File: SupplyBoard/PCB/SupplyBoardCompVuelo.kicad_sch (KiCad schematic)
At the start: 3 parts, among them J1 Conn_01x02, J2 NebulaConnector, SW1 SW_SPDT

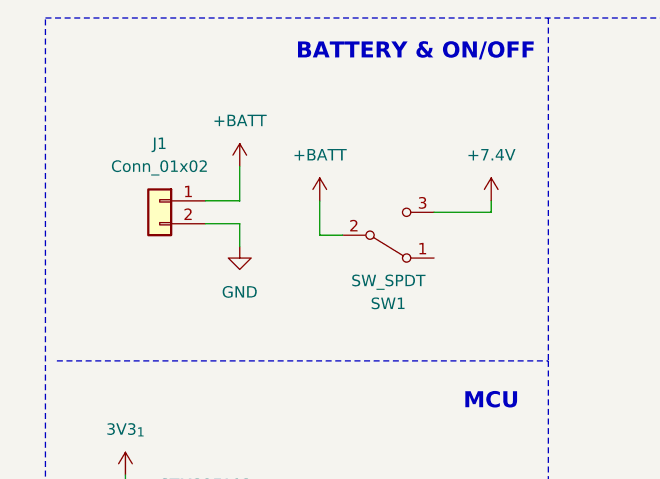
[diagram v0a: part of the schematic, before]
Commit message: Supply & Coms-Sensor Board
la organizacion de los componentes presentes en las placas, se quedaran de esa manera, se espera que en la serigrafia se incluyan los logos de los patrocinadores, ademas se incluyo la carpeta 3D la cual contiene modelos en 3D de las dos placas, con serigrafia y componentes incluidos y ya
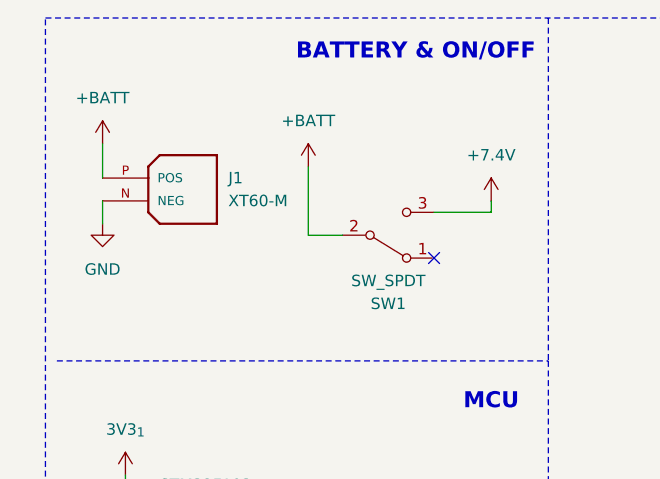
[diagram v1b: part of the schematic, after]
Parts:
- removed J1: Conn_01x02, Connector_AMASS:AMASS_XT30U-F_1x02_P5.0mm_Vertical, symbol Connector_Generic:Conn_01x02
- added J1: XT60-M, CompVuelo:AMASS_XT60-M, symbol CompVuelo:XT60-M
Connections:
- net +BATT: now also J1.P (POS)
- net GND: now also J1.N (NEG)
- no-connect marks 0 -> 1
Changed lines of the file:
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@@
 		)
+	)
+	(no_connect
+		(at 58.42 41.91)
 	)
 	(polyline
@@
 	(wire
 		(pts
-			(xy 36.83 31.75) (xy 36.83 35.56)
+			(xy 21.59 29.21) (xy 21.59 33.02)
 		)
 		(stroke
@@
 		)
 	)
+	(wire
+		(pts
+			(xy 44.45 39.37) (xy 48.26 39.37)
+		)
+		(stroke
+			(width 0)
+			(type default)
+		)
+	)
 	(polyline
 		(pts
@@
 	(wire
 		(pts
-			(xy 36.83 38.1) (xy 33.02 38.1)
-		)
-		(stroke
-			(width 0)
-			(type default)
-		)
-	)
-	(wire
-		(pts
 			(xy 132.08 48.26) (xy 129.54 48.26)
 		)
@@
 	(wire
 		(pts
-			(xy 36.83 35.56) (xy 33.02 35.56)
-		)
-		(stroke
-			(width 0)
-			(type default)
-		)
-	)
-	(wire
-		(pts
 			(xy 58.42 36.83) (xy 64.77 36.83)
 		)
@@
 		(pts
 			(xy 57.15 72.39) (xy 55.88 72.39)
-		)
-		(stroke
-			(width 0)
-			(type default)
-		)
-	)
-	(wire
-		(pts
-			(xy 45.72 39.37) (xy 48.26 39.37)
 		)
 		(stroke
@@
 	(wire
 		(pts
-			(xy 45.72 35.56) (xy 45.72 39.37)
-		)
-		(stroke
-			(width 0)
-			(type default)
-		)
-	)
-	(wire
-		(pts
-			(xy 36.83 38.1) (xy 36.83 40.64)
+			(xy 44.45 31.75) (xy 44.45 39.37)
+		)
+		(stroke
+			(width 0)
+			(type default)
+		)
+	)
+	(wire
+		(pts
+			(xy 21.59 35.56) (xy 21.59 38.1)
 		)
 		(stroke
@@
 	)
 	(symbol
+		(lib_id "CompVuelo:XT60-M")
+		(at 26.67 35.56 0)
+		(unit 1)
+		(exclude_from_sim no)
+		(in_bom yes)
+		(on_board yes)
+		(dnp no)
+		(fields_autoplaced yes)
+		(property "Reference" "J1"
+			(at 35.56 33.0199 0)
+			(effects
+				(font
+					(size 1.27 1.27)
+				)
+				(justify left)
+			)
+		)
+		(property "Value" "XT60-M"
+			(at 35.56 35.5599 0)
+			(effects
+				(font
+					(size 1.27 1.27)
+				)
+				(justify left)
+			)
+		)
+		(property "Footprint" "CompVuelo:AMASS_XT60-M"
+			(at 26.67 35.56 0)
+			(effects
+				(font
+					(size 1.27 1.27)
+				)
+				(justify bottom)
+				(hide yes)
+			)
+		)
+		(property "Datasheet" ""
+			(at 26.67 35.56 0)
+			(effects
+				(font
+					(size 1.27 1.27)
+				)
+				(hide yes)
+			)
+		)
+		(property "Description" ""
+			(at 26.67 35.56 0)
+			(effects
+				(font
+					(size 1.27 1.27)
+				)
+				(hide yes)
+			)
+		)
+		(pin "N"
+		)
+		(pin "P"
+		)
+		(instances
+			(project ""
+				(path "/2119c5ce-afa8-4b00-8fd4-fc653d4beb45"
+					(reference "J1")
+					(unit 1)
+				)
+			)
+		)
+	)
+	(symbol
 		(lib_id "power:+7.5V")
 		(at 152.4 31.75 0)
@@
 	)
 	(symbol
-		(lib_id "Connector_Generic:Conn_01x02")
-		(at 27.94 35.56 0)
-		(mirror y)
+		(lib_id "power:+BATT")
+		(at 21.59 29.21 0)
 		(unit 1)
 		(exclude_from_sim no)
@@
 		(dnp no)
 		(fields_autoplaced yes)
-		(property "Reference" "J1"
-			(at 27.94 29.21 0)
-			(effects
-				(font
-					(size 1.27 1.27)
-				)
-			)
-		)
-		(property "Value" "Conn_01x02"
-			(at 27.94 31.75 0)
-			(effects
-				(font
-					(size 1.27 1.27)
-				)
-			)
-		)
-		(property "Footprint" "Connector_AMASS:AMASS_XT30U-F_1x02_P5.0mm_Vertical"
-			(at 27.94 35.56 0)
-			(effects
-				(font
-					(size 1.27 1.27)
-				)
-				(hide yes)
-			)
-		)
-		(property "Datasheet" "~"
-			(at 27.94 35.56 0)
-			(effects
-				(font
-					(size 1.27 1.27)
-				)
-				(hide yes)
-			)
-		)
-		(property "Description" "Generic connector, single row, 01x02, script generated (kicad-library-utils/schlib/autogen/connector/)"
-			(at 27.94 35.56 0)
-			(effects
-				(font
-					(size 1.27 1.27)
-				)
-				(hide yes)
-			)
-		)
-		(pin "2"
+		(property "Reference" "#PWR03"
+			(at 21.59 33.02 0)
+			(effects
+				(font
+					(size 1.27 1.27)
+				)
+				(hide yes)
+			)
+		)
+		(property "Value" "+BATT"
+			(at 21.59 24.13 0)
+			(effects
+				(font
+					(size 1.27 1.27)
+				)
+			)
+		)
+		(property "Footprint" ""
+			(at 21.59 29.21 0)
+			(effects
+				(font
+					(size 1.27 1.27)
+				)
+				(hide yes)
+			)
+		)
+		(property "Datasheet" ""
+			(at 21.59 29.21 0)
+			(effects
+				(font
+					(size 1.27 1.27)
+				)
+				(hide yes)
+			)
+		)
+		(property "Description" "Power symbol creates a global label with name \"+BATT\""
+			(at 21.59 29.21 0)
+			(effects
+				(font
+					(size 1.27 1.27)
+				)
+				(hide yes)
+			)
 		)
 		(pin "1"
@@
 			(project ""
 				(path "/2119c5ce-afa8-4b00-8fd4-fc653d4beb45"
-					(reference "J1")
+					(reference "#PWR03")
 					(unit 1)
 				)
@@
 	)
 	(symbol
-		(lib_id "power:+BATT")
-		(at 36.83 31.75 0)
+		(lib_id "power:GND")
+		(at 21.59 38.1 0)
 		(unit 1)
 		(exclude_from_sim no)
@@
 		(dnp no)
 		(fields_autoplaced yes)
-		(property "Reference" "#PWR03"
-			(at 36.83 35.56 0)
-			(effects
-				(font
-					(size 1.27 1.27)
-				)
-				(hide yes)
-			)
-		)
-		(property "Value" "+BATT"
-			(at 36.83 26.67 0)
+		(property "Reference" "#PWR04"
+			(at 21.59 44.45 0)
+			(effects
+				(font
+					(size 1.27 1.27)
+				)
+				(hide yes)
+			)
+		)
+		(property "Value" "GND"
+			(at 21.59 43.18 0)
 			(effects
 				(font
@@
 		)
 		(property "Footprint" ""
-			(at 36.83 31.75 0)
+			(at 21.59 38.1 0)
 			(effects
 				(font
@@
 		)
 		(property "Datasheet" ""
-			(at 36.83 31.75 0)
-			(effects
-				(font
-					(size 1.27 1.27)
-				)
-				(hide yes)
-			)
-		)
-		(property "Description" "Power symbol creates a global label with name \"+BATT\""
-			(at 36.83 31.75 0)
-			(effects
-				(font
-					(size 1.27 1.27)
-				)
-				(hide yes)
-			)
-		)
-		(pin "1"
-		)
-		(instances
-			(project ""
-				(path "/2119c5ce-afa8-4b00-8fd4-fc653d4beb45"
-					(reference "#PWR03")
-					(unit 1)
-				)
-			)
-		)
-	)
-	(symbol
-		(lib_id "power:GND")
-		(at 36.83 40.64 0)
-		(unit 1)
-		(exclude_from_sim no)
-		(in_bom yes)
-		(on_board yes)
-		(dnp no)
-		(fields_autoplaced yes)
-		(property "Reference" "#PWR04"
-			(at 36.83 46.99 0)
-			(effects
-				(font
-					(size 1.27 1.27)
-				)
-				(hide yes)
-			)
-		)
-		(property "Value" "GND"
-			(at 36.83 45.72 0)
-			(effects
-				(font
-					(size 1.27 1.27)
-				)
-			)
-		)
-		(property "Footprint" ""
-			(at 36.83 40.64 0)
-			(effects
-				(font
-					(size 1.27 1.27)
-				)
-				(hide yes)
-			)
-		)
-		(property "Datasheet" ""
-			(at 36.83 40.64 0)
+			(at 21.59 38.1 0)
 			(effects
 				(font
@@
 		)
 		(property "Description" "Power symbol creates a global label with name \"GND\" , ground"
-			(at 36.83 40.64 0)
+			(at 21.59 38.1 0)
 			(effects
 				(font
@@
 	(symbol
 		(lib_id "power:+BATT")
-		(at 45.72 35.56 0)
+		(at 44.45 31.75 0)
 		(unit 1)
 		(exclude_from_sim no)
@@
 		(fields_autoplaced yes)
 		(property "Reference" "#PWR05"
-			(at 45.72 39.37 0)
+			(at 44.45 35.56 0)
 			(effects
 				(font
@@
 		)
 		(property "Value" "+BATT"
-			(at 45.72 30.48 0)
+			(at 44.45 26.67 0)
 			(effects
 				(font
@@
 		)
 		(property "Footprint" ""
-			(at 45.72 35.56 0)
+			(at 44.45 31.75 0)
 			(effects
 				(font
@@
 		)
 		(property "Datasheet" ""
-			(at 45.72 35.56 0)
+			(at 44.45 31.75 0)
 			(effects
 				(font
@@
 		)
 		(property "Description" "Power symbol creates a global label with name \"+BATT\""
-			(at 45.72 35.56 0)
-			(effects
-				(font
+			(at 44.45 31.75 0)
+			(effects
+				(font
